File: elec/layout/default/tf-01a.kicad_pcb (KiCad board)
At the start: 2 copper layers, 225.7 x 100.8 mm, 0 parts

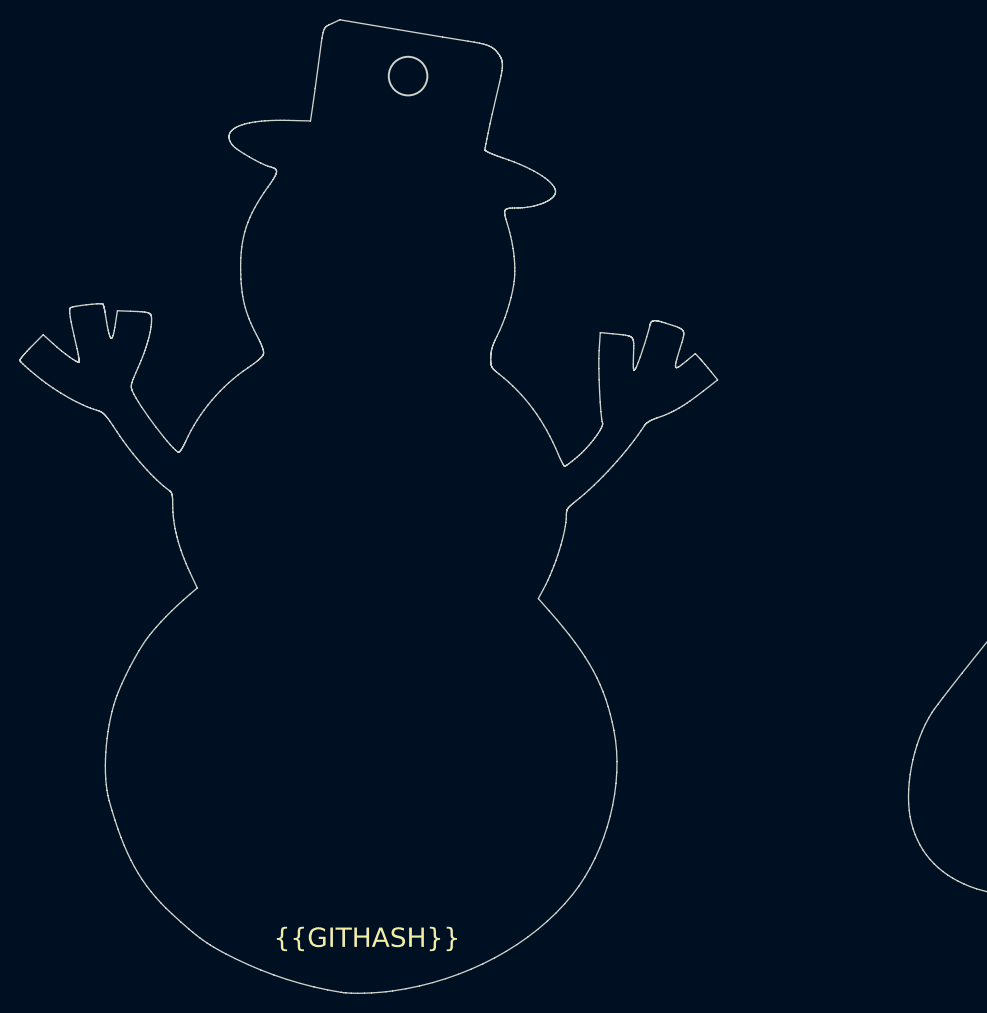
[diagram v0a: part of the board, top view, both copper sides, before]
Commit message: connect case to gnd
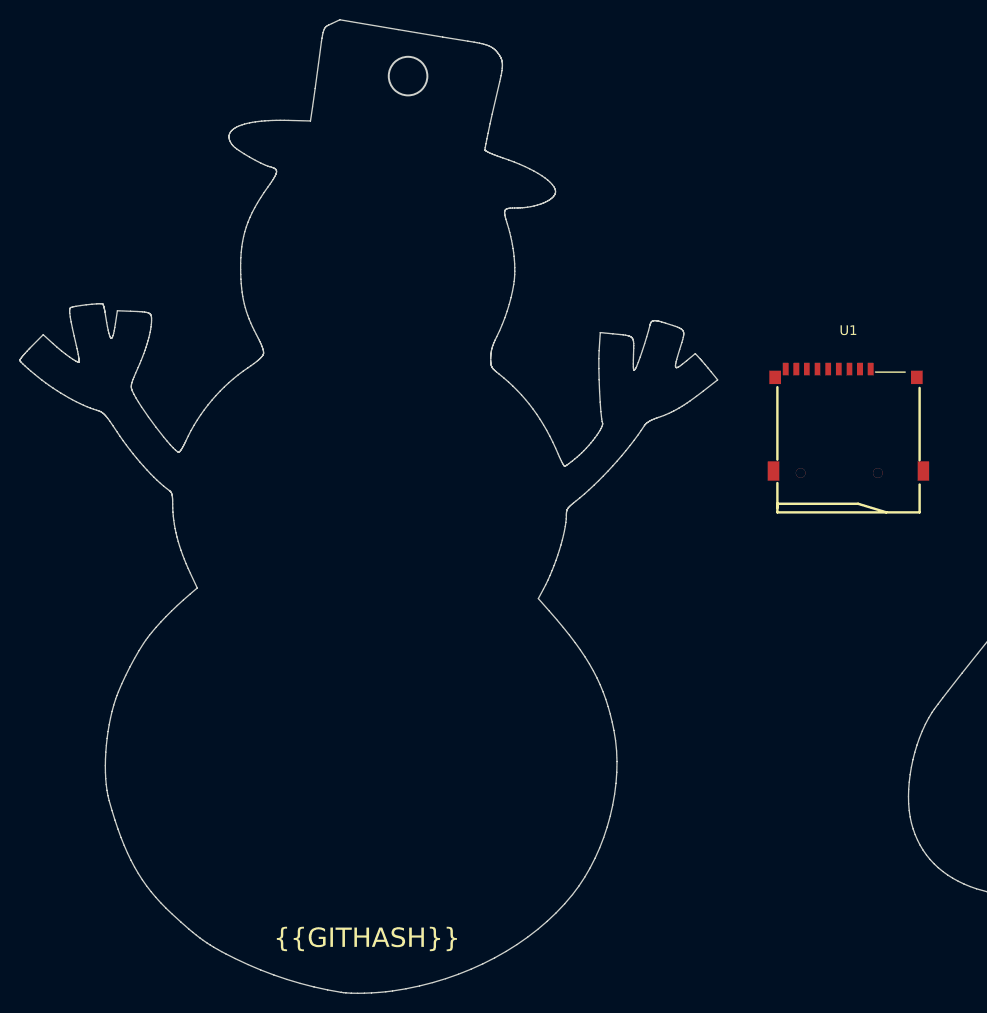
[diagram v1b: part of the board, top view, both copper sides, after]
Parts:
- added U1: , lib:TF-SMD_TF-01A, F.Cu at (121.8, 91.2)
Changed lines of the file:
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@@
   )
   (net 0 "")
+  (net 1 "dat2_rsv_")
+  (net 2 "cddat3_cs_")
+  (net 3 "cmd_di_")
+  (net 4 "vdd")
+  (net 5 "clk_sclk_")
+  (net 6 "vss")
+  (net 7 "dat0_d0_")
+  (net 8 "dat1_rsv_")
+  (net 9 "cd")
+  (net 10 "gnd")
+  (footprint "lib:TF-SMD_TF-01A" (layer "F.Cu")
+    (at 121.78 91.24)
+    (attr smd)
+    (fp_text reference "U1" (at 0 -9.28) (layer "F.SilkS")
+        (effects (font (size 1 1) (thickness 0.15)))
+    )
+    (fp_text value "" (at 0 9.28) (layer "F.Fab")
+        (effects (font (size 1 1) (thickness 0.15)))
+    )
+    (fp_text user "${REFERENCE}" (at 0 0) (layer "F.Fab")
+        (effects (font (size 1 1) (thickness 0.15)))
+    )
+    (fp_line (start -7.36 -3.41) (end -7.36 4.1)
+      (stroke (width 0.25) (type solid)) (layer "F.SilkS"))
+    (fp_line (start -7.36 6.52) (end -7.36 9.56)
+      (stroke (width 0.25) (type solid)) (layer "F.SilkS"))
+    (fp_line (start -7.36 8.67) (end 1 8.67)
+      (stroke (width 0.25) (type solid)) (layer "F.SilkS"))
+    (fp_line (start -7.36 9.09) (end -7.36 8.67)
+      (stroke (width 0.25) (type solid)) (layer "F.SilkS"))
+    (fp_line (start -7.36 9.56) (end 7.37 9.56)
+      (stroke (width 0.25) (type solid)) (layer "F.SilkS"))
+    (fp_line (start 1 8.67) (end 3.94 9.56)
+      (stroke (width 0.25) (type solid)) (layer "F.SilkS"))
+    (fp_line (start 2.79 -4.97) (end 5.89 -4.97)
+      (stroke (width 0.1) (type solid)) (layer "F.SilkS"))
+    (fp_line (start 7.37 4.17) (end 7.37 -3.33)
+      (stroke (width 0.25) (type solid)) (layer "F.SilkS"))
+    (fp_line (start 7.37 9.56) (end 7.37 6.67)
+      (stroke (width 0.25) (type solid)) (layer "F.SilkS"))
+    (fp_circle (center -4.95 5.48) (end -4.75 5.48)
+      (stroke (width 0.4) (type solid)) (fill none) (layer "Cmts.User"))
+    (fp_circle (center 3.05 5.48) (end 3.25 5.48)
+      (stroke (width 0.4) (type solid)) (fill none) (layer "Cmts.User"))
+    (fp_circle (center 8.05 -5.47) (end 8.08 -5.47)
+      (stroke (width 0.06) (type solid)) (fill none) (layer "F.Fab"))
+    (pad "" thru_hole circle (at -4.95 5.48) (size 1 1) (drill 1) (layers "*.Cu" "*.Mask"))
+    (pad "" thru_hole circle (at 3.05 5.48) (size 1 1) (drill 1) (layers "*.Cu" "*.Mask"))
+    (pad "1" smd rect (at 2.3 -5.28) (size 0.6 1.3) (layers "F.Cu" "F.Paste" "F.Mask")
+      (net 1 "dat2_rsv_") (pintype "stereo"))
+    (pad "2" smd rect (at 1.2 -5.28) (size 0.6 1.3) (layers "F.Cu" "F.Paste" "F.Mask")
+      (net 2 "cddat3_cs_") (pintype "stereo"))
+    (pad "3" smd rect (at 0.1 -5.28) (size 0.6 1.3) (layers "F.Cu" "F.Paste" "F.Mask")
+      (net 3 "cmd_di_") (pintype "stereo"))
+    (pad "4" smd rect (at -1 -5.28) (size 0.6 1.3) (layers "F.Cu" "F.Paste" "F.Mask")
+      (net 4 "vdd") (pintype "stereo"))
+    (pad "5" smd rect (at -2.1 -5.28) (size 0.6 1.3) (layers "F.Cu" "F.Paste" "F.Mask")
+      (net 5 "clk_sclk_") (pintype "stereo"))
+    (pad "6" smd rect (at -3.2 -5.28) (size 0.6 1.3) (layers "F.Cu" "F.Paste" "F.Mask")
+      (net 6 "vss") (pintype "stereo"))
+    (pad "7" smd rect (at -4.3 -5.28) (size 0.6 1.3) (layers "F.Cu" "F.Paste" "F.Mask")
+      (net 7 "dat0_d0_") (pintype "stereo"))
+    (pad "8" smd rect (at -5.4 -5.28) (size 0.6 1.3) (layers "F.Cu" "F.Paste" "F.Mask")
+      (net 8 "dat1_rsv_") (pintype "stereo"))
+    (pad "9" smd rect (at -6.5 -5.28) (size 0.6 1.3) (layers "F.Cu" "F.Paste" "F.Mask")
+      (net 9 "cd") (pintype "stereo"))
+    (pad "10" smd rect (at -7.6 -4.43) (size 1.2 1.4) (layers "F.Cu" "F.Paste" "F.Mask")
+      (net 10 "gnd") (pintype "stereo"))
+    (pad "11" smd rect (at -7.76 5.28) (size 1.2 2) (layers "F.Cu" "F.Paste" "F.Mask")
+      (net 10 "gnd") (pintype "stereo"))
+    (pad "12" smd rect (at 7.76 5.28) (size 1.2 2) (layers "F.Cu" "F.Paste" "F.Mask")
+      (net 10 "gnd") (pintype "stereo"))
+    (pad "13" smd rect (at 7.08 -4.43) (size 1.2 1.4) (layers "F.Cu" "F.Paste" "F.Mask")
+      (net 10 "gnd") (pintype "stereo"))
+    (model "/Users/narayanpowderly/Documents/atopile-workspace/the-everything-sensor/.ato/modules/tf-01a/elec/footprints/footprints.3dshapes/TF-SMD_L14.8-W14.5-H1.9-P1.1.wrl"
+      (offset (xyz 0 -2.17 0.6))
+      (scale (xyz 1 1 1))
+      (rotate (xyz 0 0 0))
+    )
+  )
   (gr_circle (center 225.62 81.79) (end 227.32 81.79)
     (stroke (width 0.1) (type solid)) (fill none) (layer "Edge.Cuts"))
@@
       (xy 69.100734 49.778315)
     )
-    (stroke (width 0) (type solid)) (fill none) (layer "Edge.Cuts"))
+    (stroke (width 0.1) (type solid)) (fill none) (layer "Edge.Cuts"))
   (gr_arc (start 261.62 113.79) (mid 260.448427 116.618427) (end 257.62 117.79)
     (stroke (width 0.1) (type solid)) (layer "Edge.Cuts"))
